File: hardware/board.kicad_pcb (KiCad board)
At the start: 2 copper layers, 60 x 50 mm, 67 parts, among them J1 Conn_01x06_Female, J2 Conn_01x06_Female, Q1 AO3400A, SW1 BTN1, SW2 BTN2, SW3 BTN3, U1 HT7833-1-SOT89, U2 ATmega328PB-AU, U4 74HC595, U5 74HC595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

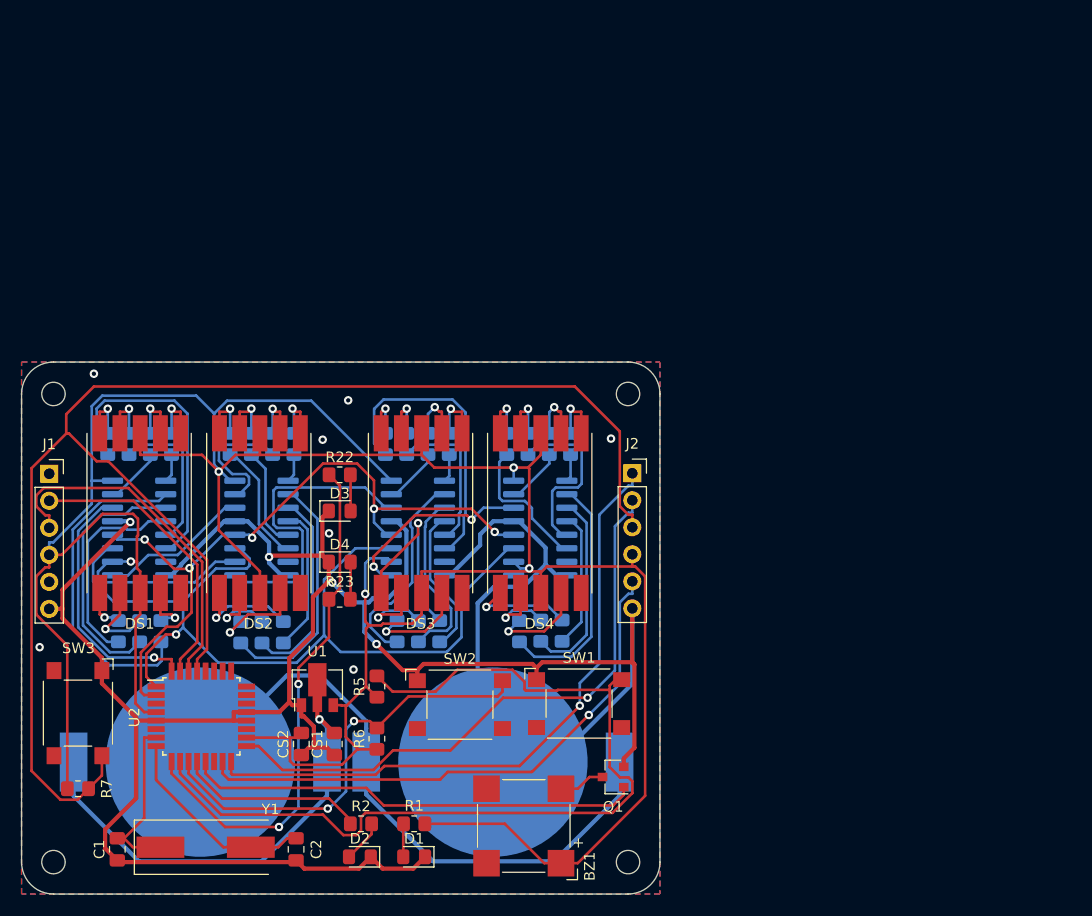
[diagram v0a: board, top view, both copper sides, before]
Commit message: Folder reorganized: hardware
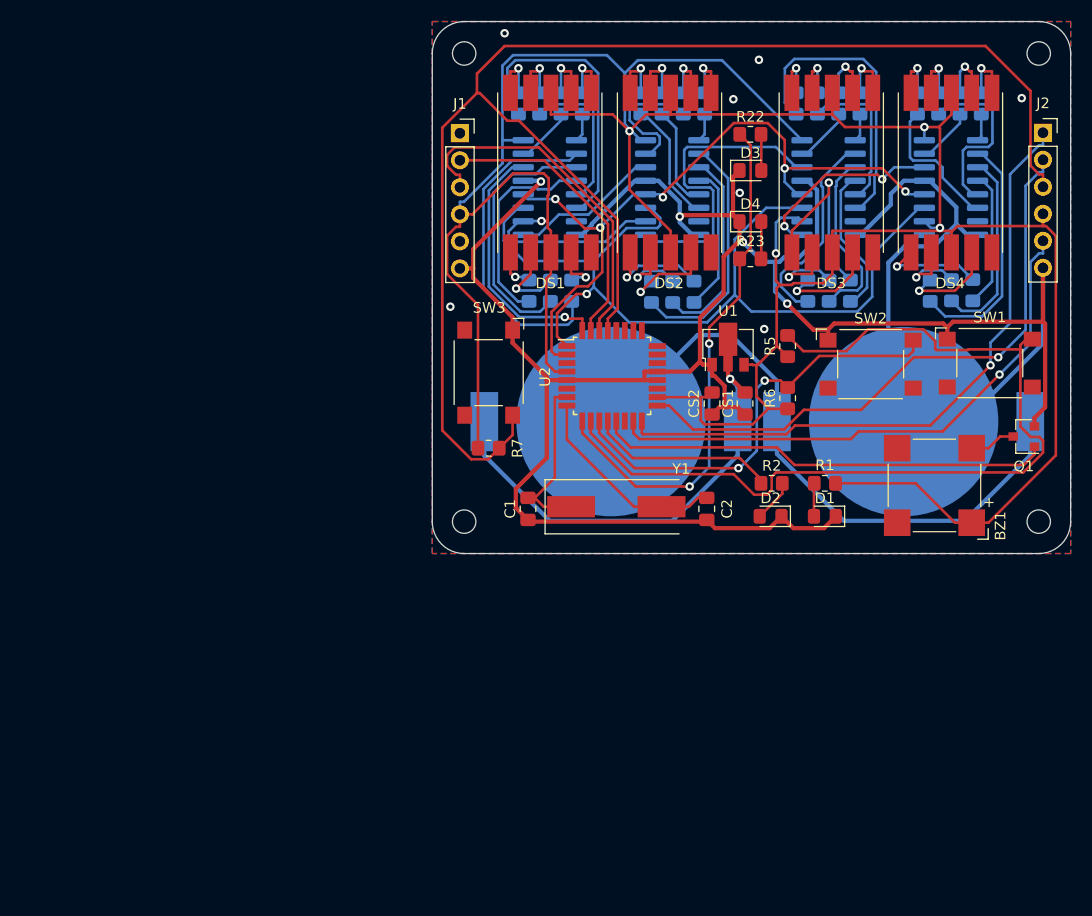
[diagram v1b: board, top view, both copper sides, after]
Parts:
- moved DS4 50.1 mm to (167.3, 75.6)
- moved C1 50.1 mm to (127.6, 116.8)
- moved C2 50.1 mm to (144.4, 116.8)
- moved R10 50.1 mm to (131.7, 96.3)
- moved R11 50.1 mm to (129.7, 96.3)
- moved R12 50.1 mm to (127.7, 96.3)
- moved R26 50.1 mm to (153.9, 96.3)
- moved R27 50.1 mm to (155.9, 96.3)
- moved R28 50.1 mm to (157.9, 96.3)
- moved R33 50.1 mm to (165.4, 96.3)
- moved U2 50.1 mm to (135.5, 104.3)
- moved BT1 50.1 mm to (135.4, 108.6)
- moved BT2 50.1 mm to (162.9, 108.6)
- moved BZ1 50.1 mm to (165.8, 114.6)
- moved CS2 50.1 mm to (144.9, 106.9)
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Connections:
- net /BATT_3V renamed Net-(BT1-Pad2)
